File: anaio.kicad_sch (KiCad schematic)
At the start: 8 parts, among them J42 Conn_01x04, J43 Conn_01x02, J44 Conn_01x02, J45 Conn_01x04, J46 Conn_01x02, J47 Conn_01x02, U23 TCA9535PWR(UMW)

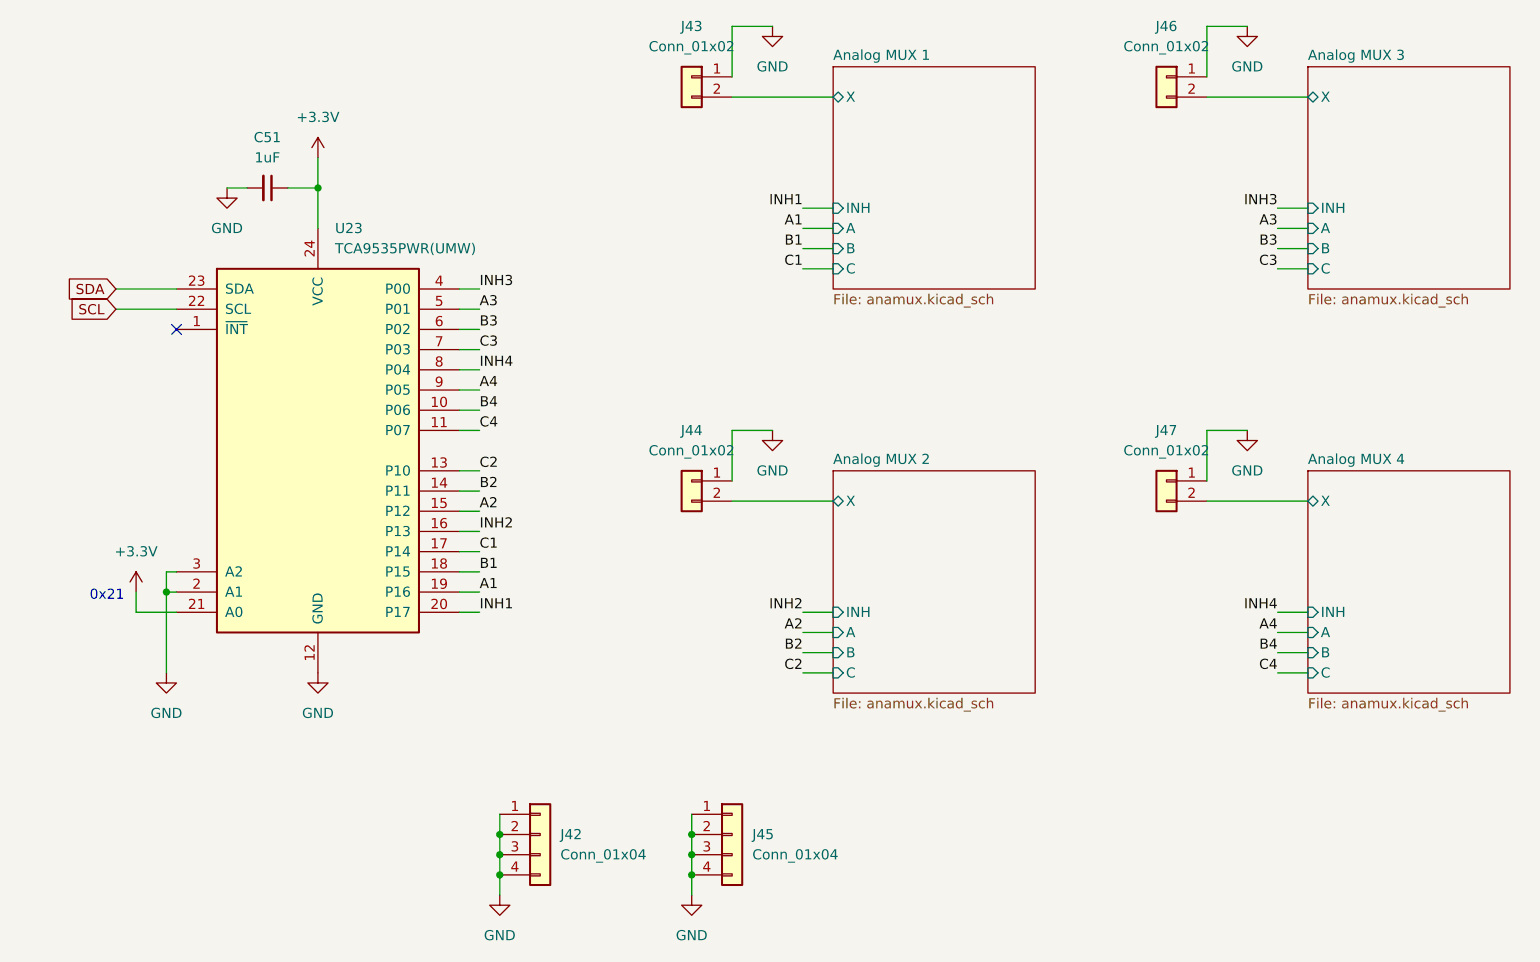
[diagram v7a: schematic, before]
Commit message: Update anamux labeling and title blocks
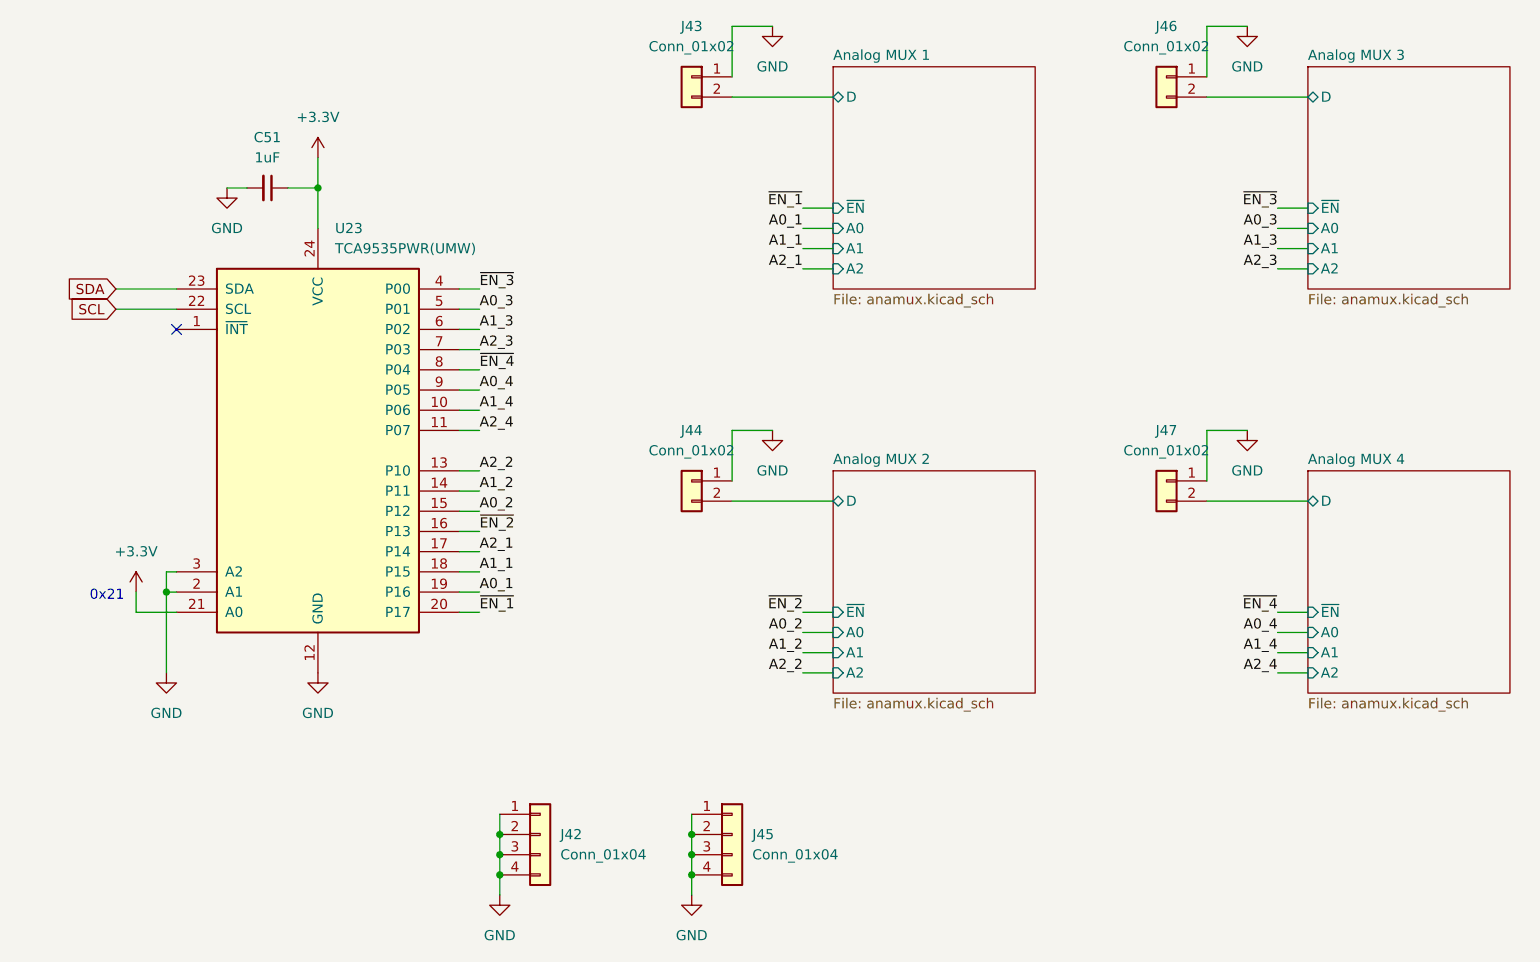
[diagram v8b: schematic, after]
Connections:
- net A1 renamed A0_1
- net A2 renamed A0_2
- net A3 renamed A0_3
- net A4 renamed A0_4
- net Analog MUX 1/X renamed Analog MUX 1/D
- net Analog MUX 2/X renamed Analog MUX 2/D
- net Analog MUX 3/X renamed Analog MUX 3/D
- net Analog MUX 4/X renamed Analog MUX 4/D
- net B1 renamed A1_1
- net B2 renamed A1_2
- net B3 renamed A1_3
- net B4 renamed A1_4
- net C1 renamed A2_1
- net C2 renamed A2_2
- net C3 renamed A2_3
- net C4 renamed A2_4
- net INH1 renamed ~{EN_1}
- net INH2 renamed ~{EN_2}
- net INH3 renamed ~{EN_3}
- net INH4 renamed ~{EN_4}
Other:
- sheet Analog MUX 1 ports: added A0, A1, A2, D, ~{EN}; removed A, B, C, INH, X
- sheet Analog MUX 2 ports: added A0, A1, A2, D, ~{EN}; removed A, B, C, INH, X
- sheet Analog MUX 3 ports: added A0, A1, A2, D, ~{EN}; removed A, B, C, INH, X
- sheet Analog MUX 4 ports: added A0, A1, A2, D, ~{EN}; removed A, B, C, INH, X
